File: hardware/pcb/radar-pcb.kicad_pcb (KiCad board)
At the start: 2 copper layers, 66 x 128 mm, 40 parts, among them J1 DC 5,5x2,5 mm (+ w srodku), J2 DevKit J1, J3 DevKit J3, J4 HC-SR04 (kabel): VCC TRIG ECH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, J5 Serwo SG90 (kabel): GND +5V S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, J6 MAX7219 Elegoo: VCC GND DIN C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, J7 OLED SH1106: VCC GND SCK SDA, J8 Buzzer: + -, J9 Przycisk zewnetrzny, Q1 AO3401A (P-MOSFET), Q2 MMBT3904, SW1 Przycisk ON/standby, U1 SN74AHCT125N

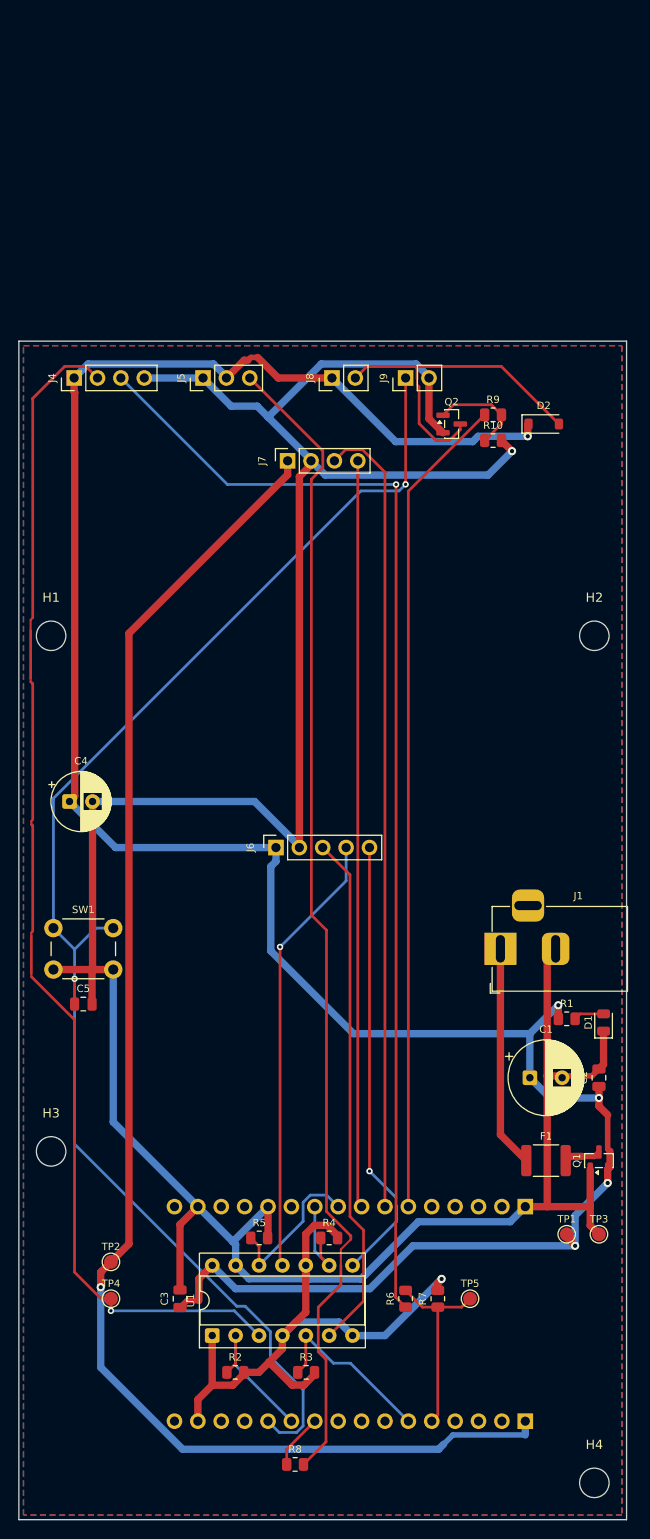
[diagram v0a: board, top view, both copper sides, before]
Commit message: PCB: silkscreen pin labels, side-actuated button, verification dimensions
Every connector is labelled with module and pin names, the DevKit sockets
with all 32 pin names on the back, parts with reference and value plus
polarity marks. ON/STANDBY uses a right-angle PTS645 switch at the left
edge. Dimensions W1-W12 to verify are drawn on Dwgs.User/Cmts.User for
the 1:1 verification PDF. DRC: 0 errors, schematic parity clean.

Co-Authored-By: Claude Opus 5.5 <noreply@anthropic.com>
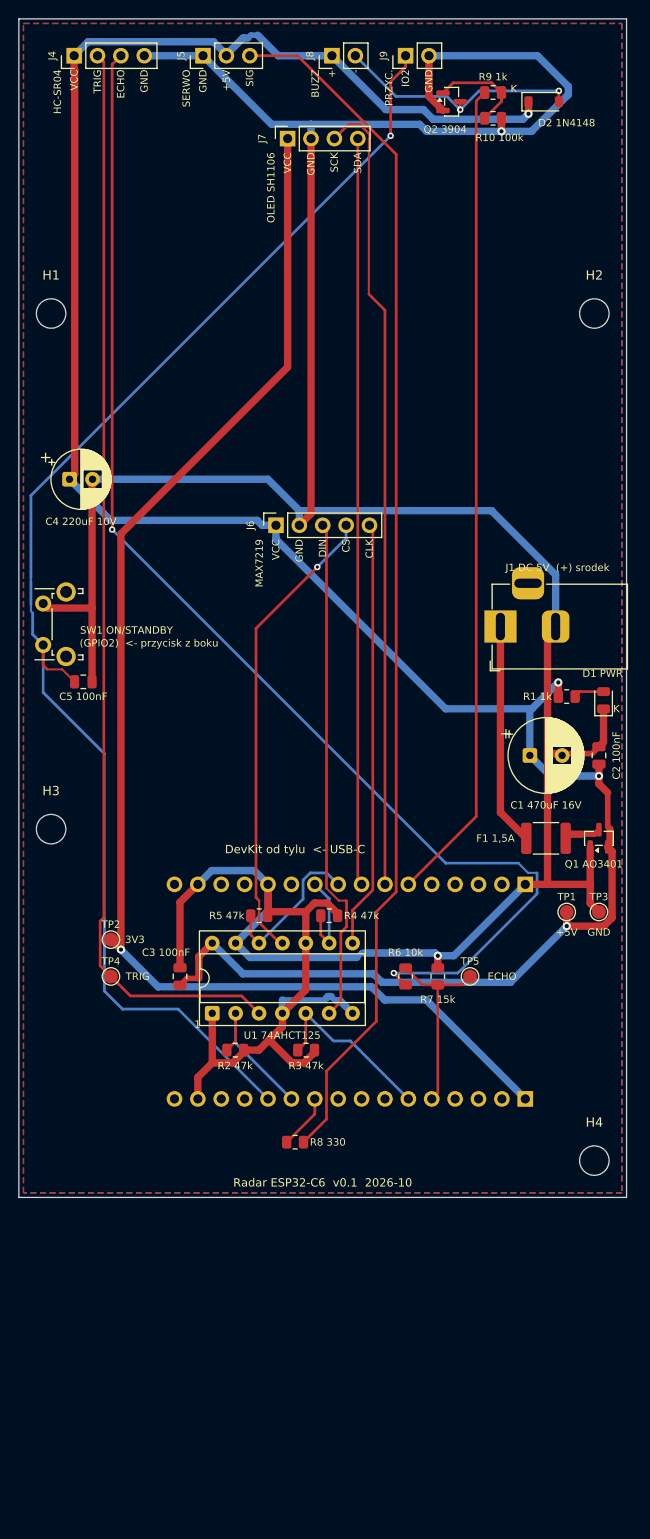
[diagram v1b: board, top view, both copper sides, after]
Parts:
- SW1: value Przycisk ON/standby -> Przycisk ON/standby (katowy); footprint Button_Switch_THT:SW_PUSH_6mm -> Button_Switch_THT:SW_Tactile_SPST_Angled_PTS645Vx58-2LFS
- moved C1 35.0 mm to (155.5, 105.0)
- moved C2 35.0 mm to (163.0, 105.0)
- moved C3 35.0 mm to (117.5, 129.0)
- moved C4 35.0 mm to (105.5, 75.0)
- moved C5 35.0 mm to (107.0, 97.0)
- moved D1 35.0 mm to (163.5, 99.0)
- moved D2 35.0 mm to (157.0, 34.0)
- moved F1 35.0 mm to (157.2, 114.0)
- moved H1 35.0 mm to (103.5, 57.0)
- moved H2 35.0 mm to (162.5, 57.0)
- moved H3 35.0 mm to (103.5, 113.0)
- moved H4 35.0 mm to (162.5, 149.0)
- moved J1 35.0 mm to (152.3, 91.0)
- moved J2 35.0 mm to (155.0, 142.3)
- moved J3 35.0 mm to (155.0, 119.0)
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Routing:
- net ECHO_5V: track 124.5 -> 136.7 mm, vias 1 -> 2
- net TRIG_5V: track 129.9 -> 118.7 mm, vias 1 -> 0
- net +3V3: track 158.8 -> 147.8 mm
- net BUZ_NEG: track 37.8 -> 27.4 mm, vias 0 -> 2
- net BTN: track 156.4 -> 150.7 mm, vias 2 -> 1
- net GND: track 382.7 -> 388.3 mm
- net SERVO_SIG: track 126.4 -> 131.8 mm
- net +5V: track 260.2 -> 257.5 mm, vias 5 -> 4
- net CS_5V: track 48.5 -> 50.8 mm
- net CLK_5V: track 48.6 -> 46.4 mm, vias 1 -> 0
- net DIN_5V: track 56.4 -> 55.3 mm
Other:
- board text added: "(GPIO2) <- przycisk z boku"
- board text added: "+"
- board text added: "+5V"
- board text added: "-"
- board text added: "1"
- board text added: "3V3"
- board text added: "5V"
- board text added: "BUZZ"
- board text added: "C1 470uF 16V"
- board text added: "C2 100nF"
- board text added: "C3 100nF"
- board text added: "C4 220uF 10V"
- board text added: "C5 100nF"
- board text added: "CLK"
- board text added: "CS"
- board text added: "D1 PWR"
- board text added: "D2 1N4148"
- board text added: "DIN"
- board text added: "DevKit J1 (pin 1 = 3V3)"
- board text added: "DevKit J3 (pin 1 = GND)"
- board text added: "DevKit od tylu <- USB-C"
- board text added: "ECHO"
- board text added: "F1 1,5A"
- board text added: "GND"
- board text added: "HC-SR04"
- board text added: "IO0"
- board text added: "IO1"
- board text added: "IO10"
- board text added: "IO11"
- board text added: "IO12"
- board text added: "IO13"
- board text added: "IO15"
- board text added: "IO18"
- board text added: "IO19"
- board text added: "IO2"
- board text added: "IO20"
- board text added: "IO21"
- board text added: "IO22"
- board text added: "IO23"
- board text added: "IO3"
- board text added: "IO4"
- board text added: "IO5"
- board text added: "IO6"
- board text added: "IO7"
- board text added: "IO8"
- board text added: "IO9"
- board text added: "J1 DC 5V (+) srodek"
- board text added: "K"
- board text added: "MAX7219"
- board text added: "NC"
- board text added: "OLED SH1106"
- board text added: "PRZYC."
- board text added: "Projekt roboczy v0.1 - NIE ZAMAWIAC przed weryfikacja wymiarow."
- board text added: "Q1 AO3401"
- board text added: "Q2 3904"
- board text added: "R1 1k"
- board text added: "R10 100k"
- board text added: "R2 47k"
- board text added: "R3 47k"
- board text added: "R4 47k"
- board text added: "R5 47k"
- board text added: "R6 10k"
- board text added: "R7 15k"
- board text added: "R8 330"
- board text added: "R9 1k"
- board text added: "RST"
- board text added: "RX"
- board text added: "Radar ESP32-C6 - tyl"
- board text added: "Radar ESP32-C6 v0.1 2026-10"
- board text added: "SCK"
- board text added: "SDA"
- board text added: "SERWO"
- board text added: "SIG"
- board text added: "SW1 ON/STANDBY"
- board text added: "Strona: PRZOD (widok od frontu)"
- board text added: "Strona: TYL (widok od tylu, lustro) - DevKit wtykany od tej strony"
- board text added: "TRIG"
- board text added: "TX"
- board text added: "U1 74AHCT125"
- board text added: "USB-C ->"
- board text added: "VCC"
- board text added: "W1 szerokosc plytki: czy miesci sie we wnetrzu kolumny obudowy"
- board text added: "W10 DevKit: rozstaw rzedow pinow (srodek-srodek), ZALOZONE 23,3 mm"
- board text added: "W11 DevKit: pin 1 - pin 16 jednej listwy (15 x 2,54 mm)"
- board text added: "W12 DevKit: od prawej krawedzi (widok od frontu) do pinu 1"
- board text added: "W2 wysokosc plytki: czy miesci sie w kolumnie nad podstawka"
- board text added: "W3 OLED: od lewej krawedzi do pinu 1 gniazda J7 (okno ekranu w obudowie)"
- board text added: "W4 MAX7219: od lewej krawedzi do pinu 1 gniazda J6 (okno matrycy)"
- board text added: "W5 odstep gniazd OLED-MAX7219 (pion), zgodny z oknami w obudowie"
- board text added: "W6 gniazdo DC: od gornej krawedzi do osi wtyku (otwor w scianie obudowy)"
- board text added: "W7 przycisk boczny: od gornej krawedzi do osi popychacza (otwor w scianie)"
- board text added: "W8 otwory montazowe M3: rozstaw w poziomie"
- board text added: "W9 otwory montazowe M3: rozstaw w pionie"
- board text added: "WYMIARY DO WERYFIKACJI (? = wartosc z projektu)"
- board text added: "Wydruk w skali 1:1 (100%, bez dopasowania do strony)."

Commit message: PCB: sonar supply RC filter, series resistors and decoupling for the matrix
Breadboard tests showed MAX7219 row switching and bus traffic causing false
HC-SR04 echoes. Adds R11 10R with C6 100uF and C7 100nF on the sonar supply,
100R series resistors R12-R14 on DIN/CLK/CS and C8/C9 at the MAX7219 socket.
DRC with schematic parity: 0 errors. Adds export_docs.sh for renders and the
verification PDF.

Co-Authored-By: Claude Opus 5.5 <noreply@anthropic.com>
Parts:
- added C6: 100 uF / 16 V, Capacitor_THT:CP_Radial_D6.3mm_P2.50mm, F.Cu at (104.5, 39.0)
- added C7: 100 nF, Capacitor_SMD:C_0805_2012Metric, F.Cu at (111.0, 39.5)
- added C8: 100 uF / 16 V, Capacitor_THT:CP_Radial_D6.3mm_P2.50mm, F.Cu at (152.2, 80.0)
- added C9: 100 nF, Capacitor_SMD:C_0805_2012Metric, F.Cu at (161.5, 80.0)
- added R11: 10, Resistor_SMD:R_0805_2012Metric, F.Cu at (116.5, 37.0)
- added R12: 100, Resistor_SMD:R_0805_2012Metric, F.Cu at (127.0, 76.0)
- added R13: 100, Resistor_SMD:R_0805_2012Metric, F.Cu at (144.0, 76.0)
- added R14: 100, Resistor_SMD:R_0805_2012Metric, F.Cu at (135.5, 76.0)
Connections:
- J4 pad 1: +5V -> SR04_VCC
- J6 pad 3: DIN_5V -> DIN_J
- J6 pad 4: CS_5V -> CS_J
- J6 pad 5: CLK_5V -> CLK_J
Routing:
- net SR04_VCC: track 0.00 -> 27.6 mm
- net +5V: track 257.5 -> 273.5 mm, vias 4 -> 6
- net BTN: track 150.7 -> 163.8 mm, vias 1 -> 2
- net CS_5V: track 50.8 -> 61.7 mm, vias 1 -> 0
- net TRIG_5V: track 118.7 -> 128.3 mm, vias 0 -> 1
- net CLK_5V: track 46.4 -> 55.3 mm
- net CLK_J: track 0.00 -> 8.49 mm
- net DIN_J: track 0.00 -> 7.48 mm
- net DIN_5V: track 55.3 -> 62.0 mm
- net GND: track 388.3 -> 394.3 mm, vias 2 -> 3
- net SERVO_SIG: track 131.8 -> 136.8 mm
- net SCL: track 87.1 -> 91.8 mm
- net ECHO_5V: track 136.7 -> 141.2 mm, vias 2 -> 1
- net CS_J: track 0.00 -> 4.36 mm
- net SDA: track 81.2 -> 83.3 mm
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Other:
- board text added: "C6 100uF"
- board text added: "C7 100nF"
- board text added: "C8 100uF"
- board text added: "C9 100nF"
- board text added: "R11 10R"
- board text added: "R12 100R"
- board text added: "R13 100R"
- board text added: "R14 100R"

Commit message: PCB: servo supply isolation and decoupling, servo signal pull-down, buzzer decoupling
Co-Authored-By: Claude Sonnet 5.5 <noreply@anthropic.com>
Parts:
- added C10: 100 nF, Capacitor_SMD:C_0805_2012Metric, F.Cu at (119.0, 33.3)
- added C11: 100 nF, Capacitor_SMD:C_0805_2012Metric, F.Cu at (139.0, 34.2)
- added C12: 100 nF (opcja), Capacitor_SMD:C_0805_2012Metric, F.Cu at (143.5, 37.5)
- added FB1: Ferryt >=1 A lub 0 R, Inductor_SMD:L_0805_2012Metric, F.Cu at (127.8, 33.4)
- added R15: 10 k, Resistor_SMD:R_0805_2012Metric, F.Cu at (129.2, 30.0)
- moved C4 41.2 mm to (122.5, 37.5)
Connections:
- C4 pad 1: +5V -> SERVO_5V
- J5 pad 2: +5V -> SERVO_5V
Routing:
- net GND: track 394.3 -> 416.6 mm, vias 3 -> 2
- net SERVO_5V: track 0.00 -> 20.6 mm
- net ECHO_5V: track 141.2 -> 121.9 mm
- net BTN: track 163.8 -> 182.1 mm, vias 2 -> 1
- net SERVO_SIG: track 136.8 -> 128.7 mm, vias 0 -> 2
- net BUZ_NEG: track 28.0 -> 34.3 mm, vias 3 -> 2
- net CS_5V: track 61.7 -> 55.7 mm, vias 0 -> 2
- net SCL: track 91.8 -> 87.4 mm
- net +5V: track 273.5 -> 271.2 mm, vias 6 -> 3
- net CLK_5V: track 55.3 -> 57.6 mm
- net SDA: track 83.3 -> 81.7 mm
- net DIN_5V: track 62.0 -> 62.8 mm, vias 0 -> 1
- net TRIG_5V: track 128.3 -> 127.4 mm
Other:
- board text added: "C10 100nF"
- board text added: "C11 100nF"
- board text added: "C12 100nF opcja"
- board text added: "FB1 ferryt/0R"
- board text added: "R15 10k"

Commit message: PCB: spread servo/buzzer parts and labels in the top area
Co-Authored-By: Claude Sonnet 5.5 <noreply@anthropic.com>
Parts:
- moved C10 12.1 mm to (114.5, 44.5)
- moved C11 8.75 mm to (144.5, 41.0), turned to 0 degrees
- moved C12 8.28 mm to (151.0, 41.0)
- moved C4 8.14 mm to (121.0, 45.5)
- moved FB1 5.87 mm to (123.5, 37.4)
- moved R15 0.30 mm to (129.5, 30.0)
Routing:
- net BTN: track 182.1 -> 160.1 mm
- net GND: track 416.6 -> 436.5 mm, vias 2 -> 4
- net +5V: track 271.2 -> 259.9 mm, vias 3 -> 5
- net ECHO_5V: track 121.9 -> 130.9 mm
- net SR04_VCC: track 28.0 -> 35.1 mm, vias 0 -> 2
- net SERVO_SIG: track 128.7 -> 135.6 mm, vias 2 -> 0
- net BUZ_CTRL: track 89.4 -> 96.1 mm
- net TRIG_5V: track 127.4 -> 121.5 mm
- net SCL: track 87.4 -> 93.0 mm
- net CLK_5V: track 57.6 -> 52.5 mm, vias 0 -> 1
- net SERVO_5V: track 20.6 -> 25.3 mm
- net CS_5V: track 55.7 -> 58.4 mm, vias 2 -> 1
- net SDA: track 81.7 -> 83.3 mm
- net BUZ_BASE: track 10.8 -> 9.58 mm
- net BUZ_NEG: track 34.3 -> 33.1 mm, vias 2 -> 1
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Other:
- board text added: "C10 100n"
- board text added: "C12 100n opc."
- board text added: "FB1 0R"
- board text removed: "C10 100nF"
- board text removed: "C12 100nF opcja"
- board text removed: "FB1 ferryt/0R"

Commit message: PCB: USB-C power input replaces DC jack; DevKit 5V pin tied to board 5V
Co-Authored-By: Claude Sonnet 5.5 <noreply@anthropic.com>
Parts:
- removed Q1: AO3401A (P-MOSFET), Package_TO_SOT_SMD:SOT-23
- added D3: SMAJ5.0CA (TVS 5 V), Diode_SMD:D_SMA, F.Cu at (152.2, 97.4)
- added R16: 5,1 k, Resistor_SMD:R_0805_2012Metric, F.Cu at (155.3, 92.6)
- added R17: 5,1 k, Resistor_SMD:R_0805_2012Metric, F.Cu at (155.3, 89.2)
- J1: value DC 5,5x2,5 mm (+ w srodku) -> USB-C zasilanie 5 V (GCT USB4105); footprint Connector_BarrelJack:BarrelJack_Horizontal -> Connector_USB:USB_C_Receptacle_GCT_USB4105-xx-A_16P_TopMnt_Horizontal
- moved J1 10.6 mm to (162.9, 91.0), turned to 90 degrees
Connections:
- F1 pad 2: VIN_F -> +5V
- J2 pad 14: unconnected-(J2-Pin_14-Pad14) -> +5V
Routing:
- net +5V: track 259.9 -> 273.4 mm, vias 5 -> 6
- net BTN: track 160.1 -> 148.3 mm
- net +3V3: track 147.8 -> 157.9 mm
- net CC2: track 0.00 -> 9.41 mm, vias 0 -> 2
- net GND: track 436.5 -> 445.7 mm, vias 4 -> 6
- net CC1: track 0.00 -> 9.13 mm, vias 0 -> 2
- net VIN: track 24.2 -> 31.9 mm
- net CS_5V: track 58.4 -> 64.1 mm, vias 1 -> 0
- net SCL: track 93.0 -> 87.6 mm, vias 0 -> 1
- net VIN_F: track 4.00 -> 0.00 mm
- net ECHO_5V: track 130.9 -> 133.8 mm
- net CLK_3V3: track 10.4 -> 12.3 mm
- net SERVO_SIG: track 135.6 -> 133.7 mm, vias 0 -> 2
- net SDA: track 83.3 -> 81.5 mm
- net BUZ_NEG: track 33.1 -> 34.6 mm
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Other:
- board text added: "D3 TVS"
- board text added: "J1 USB-C 5V"
- board text added: "R16 5k1"
- board text added: "R17 5k1"
- board text added: "W6 gniazdo USB-C zasilania: od gornej krawedzi do osi wtyku (otwor w scianie obudowy)"
- board text removed: "J1 DC 5V (+) srodek"
- board text removed: "Q1 AO3401"
- board text removed: "W6 gniazdo DC: od gornej krawedzi do osi wtyku (otwor w scianie obudowy)"
